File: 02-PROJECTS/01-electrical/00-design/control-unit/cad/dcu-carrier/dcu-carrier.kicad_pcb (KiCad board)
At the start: 2 copper layers, 180 x 80 mm, 169 parts, among them J1 DP-DCU DT13-06PA, J10 Teensy 4.1 socket - 2 x 24 fe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, J11 A/C pressure transducer lead 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, J12 radar alert lead - PLACEHOLDER, J2 DP-DCU-C DT13-08PA, J3 cabin NTC lead, J4 panel ribbon 2x13 IDC, keyed, J5 blower pigtail, J6 servo header, J7 servo header, J8 servo header, J9 DP-DCU-B DT13-12PA, Q1 PMV37ENEA, Q2 PMV37ENEA, Q3 SQ2351ES class, >= 40 V confi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, Q4 MMBT3904, U1 LMR36015FSCQ-Q1, U10 BTT6200-4ESA, U11 DRV8962-Q1, U12 TCA9539-Q1, U13 TCA9539-Q1, U14 BTT6050-1ERA, U15 ADS1115-Q1, U16 TPS7B4250-Q1, U2 TPS54560B-Q1, U3 TCAN1042HVDRQ1, U4 INA180A1, U5 BTS3011TE, U6 BTS3011TE, U7 BTS3011TE, U8 BTS3011TE, U9 BTT6050-1ERA

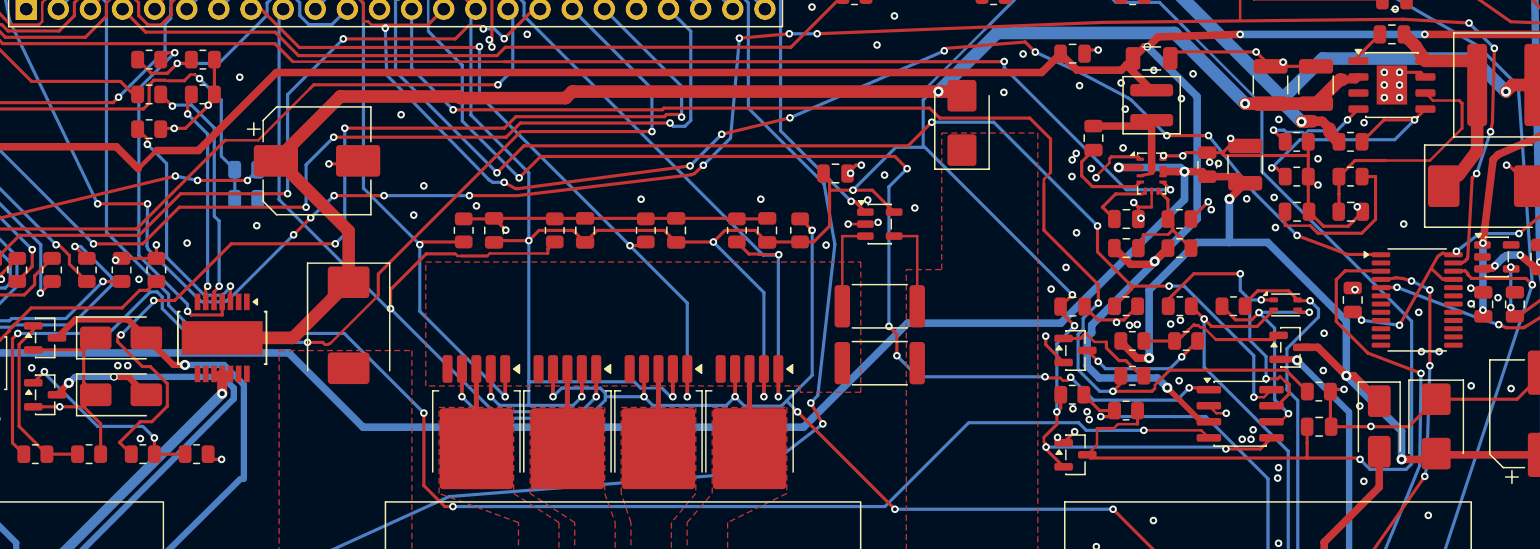
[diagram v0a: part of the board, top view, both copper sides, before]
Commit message: Electrical: the carriers corrected before the order - six TVS diodes drawn backwards, the wake switch's pins swapped, an unconnected zener, the bulk capacitor's value (D-547)
Y42 done; Y44 (an independent read of the boards, and the gate drive of two P-FETs) holds the board order Y18. DU and CU carrier fab zips rebuilt; the earlier ones must not be ordered. The board check now holds transistors and diodes to their makers' pin-outs.

Co-Authored-By: Claude Opus 5.5 <noreply@anthropic.com>
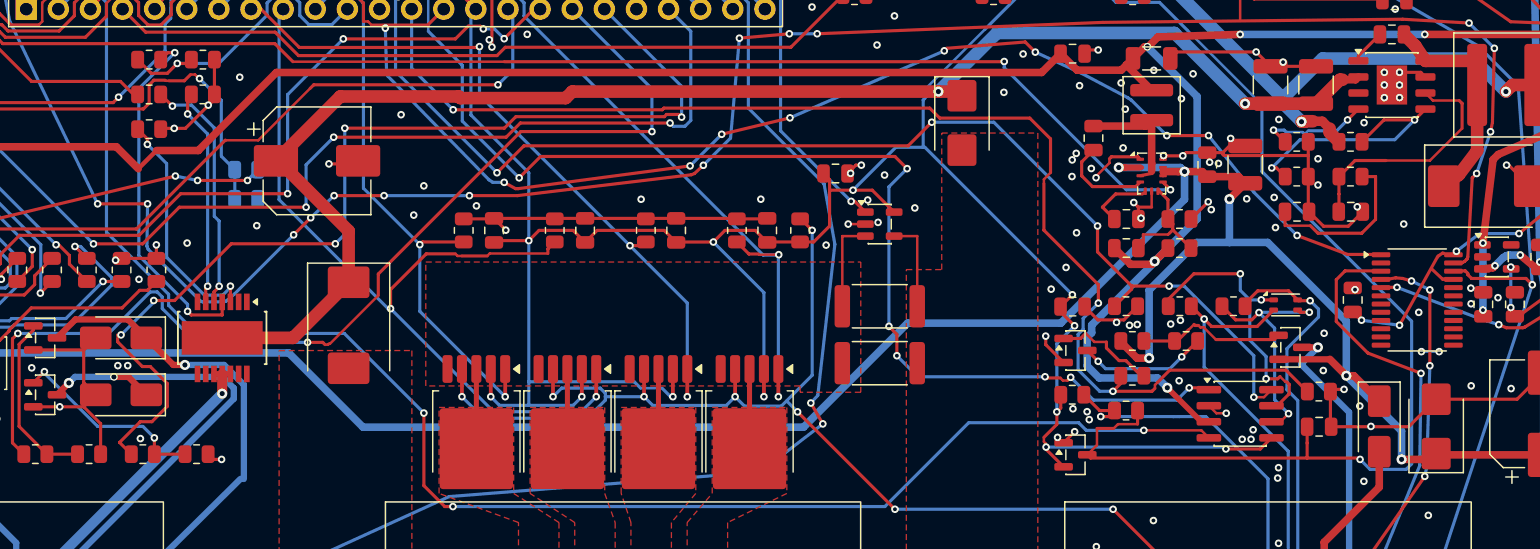
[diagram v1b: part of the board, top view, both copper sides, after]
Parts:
- C1, C29, C8: value 100u 63V -> 68u 63V
- C31, C32, C33: value 470u 10V -> 470u 16V
- Q1, Q2: value PMV37ENEA -> SQ2362CES / PMV37ENEA
- Q3: value SQ2351ES class, >= 40 V confirm -> SQ2361ES
- turned D2 to 90 degrees
- turned D4 to -90 degrees
- turned D7 to 180 degrees
- turned D8 to 180 degrees
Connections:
- D2 pad 1: GND -> +12V_LOGIC
- D2 pad 2: +12V_LOGIC -> GND
- D4 pad 1: PGND -> +12V_CMF
- D4 pad 2: +12V_CMF -> PGND
- D7 pad 1: GND -> /REL_HATCH
- D7 pad 2: /REL_HATCH -> GND
- D8 pad 1: GND -> /REL_FUEL
- D8 pad 2: /REL_FUEL -> GND
- Q3 pad 2: /WAKE_OUT -> +12V_LOGIC
- Q3 pad 3: +12V_LOGIC -> /WAKE_OUT
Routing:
- net +12V_LOGIC: track 309.9 -> 311.4 mm
- net /WAKE_OUT: track 26.8 -> 27.9 mm

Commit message: Electrical: the two P-FETs' gate drive brought down, the order text names the parts as they are (D-547)
CU Q3: R43 18 k, inside its gate limit at the 53 V clamp. DU Q1: R2 10 k, inside to 40 V on the rail; a gate zener for the clamp case is held for one fix pass with the independent review's findings (Y44). No fab file changed; the cart file follows. Y18's steps rebuilt.

Co-Authored-By: Claude Opus 5.5 <noreply@anthropic.com>
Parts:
- R43: value 1k -> 18k
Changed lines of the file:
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@@
 			)
 		)
-		(property "Value" "1k"
+		(property "Value" "18k"
 			(at 0 1.65 0)
 			(layer "F.Fab")

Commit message: Electrical: the independent read's findings fixed on the boards before the order, and the Display Unit's brake-warning input given its pull-up (D-549)
Y44 done; Y18 (the board order) opens. DU carrier rev 0.06: road-speed input IC08 re-laid, a 15 V gate zener and 4.7 k on the backlight switch, four vias at each backlight layer change, brake warning IC06 pulled up to 3V3 (found while the changes were read back - it could never have read high), tell-tale dividers 22 k, MMBT5551 and SL310A on the rails clamped at 53 V. CU carrier rev 0.07, values only: C27 100 nF, Q1 / Q2 SQ2364EES, Q4 MMBT5551, D1 SL310A. Panel: the encoders' lug slots to Bourns' layout. Two assembly drawings in each fab folder in place of silkscreen references.

ERC 0, DRC 0 / 0 / 0, check.py 0 mismatches on all five boards. The DU carrier's and the panel's fab zips are rebuilt under the same names; the CU carrier's and the upper board's are unchanged. Cart 98 lines. Record: icu_channels IC06 IC08 IC09 IC12 IC13, dcu_channels SN23 SN24, parts P106 P107 P147 P149 P169 P170 P203, Y18 / F3 / F5 briefs and steps. D-548's DT13 question is untouched (V-117).

Co-Authored-By: Claude Opus 5.5 <noreply@anthropic.com>
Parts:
- C27: value 22n 100V confirm -> 100n 100V
- D1: value SS34 -> SL310A
- Q1, Q2: value SQ2362CES / PMV37ENEA -> SQ2364EES
- Q4: value MMBT3904 -> MMBT5551
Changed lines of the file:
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@@
 			)
 		)
-		(property "Value" "SQ2362CES / PMV37ENEA"
+		(property "Value" "SQ2364EES"
 			(at 0 2.4 0)
 			(layer "F.Fab")
@@
 			)
 		)
-		(property "Value" "22n 100V  confirm"
+		(property "Value" "100n 100V"
 			(at 0 1.68 90)
 			(layer "F.Fab")
@@
 			)
 		)
-		(property "Value" "SS34"
+		(property "Value" "SL310A"
 			(at 0 2.6 270)
 			(layer "F.Fab")
@@
 			)
 		)
-		(property "Value" "SQ2362CES / PMV37ENEA"
+		(property "Value" "SQ2364EES"
 			(at 0 2.4 0)
 			(layer "F.Fab")
@@
 			)
 		)
-		(property "Value" "MMBT3904"
+		(property "Value" "MMBT5551"
 			(at 0 2.4 0)
 			(layer "F.Fab")
